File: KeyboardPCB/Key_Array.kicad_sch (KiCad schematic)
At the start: 70 parts

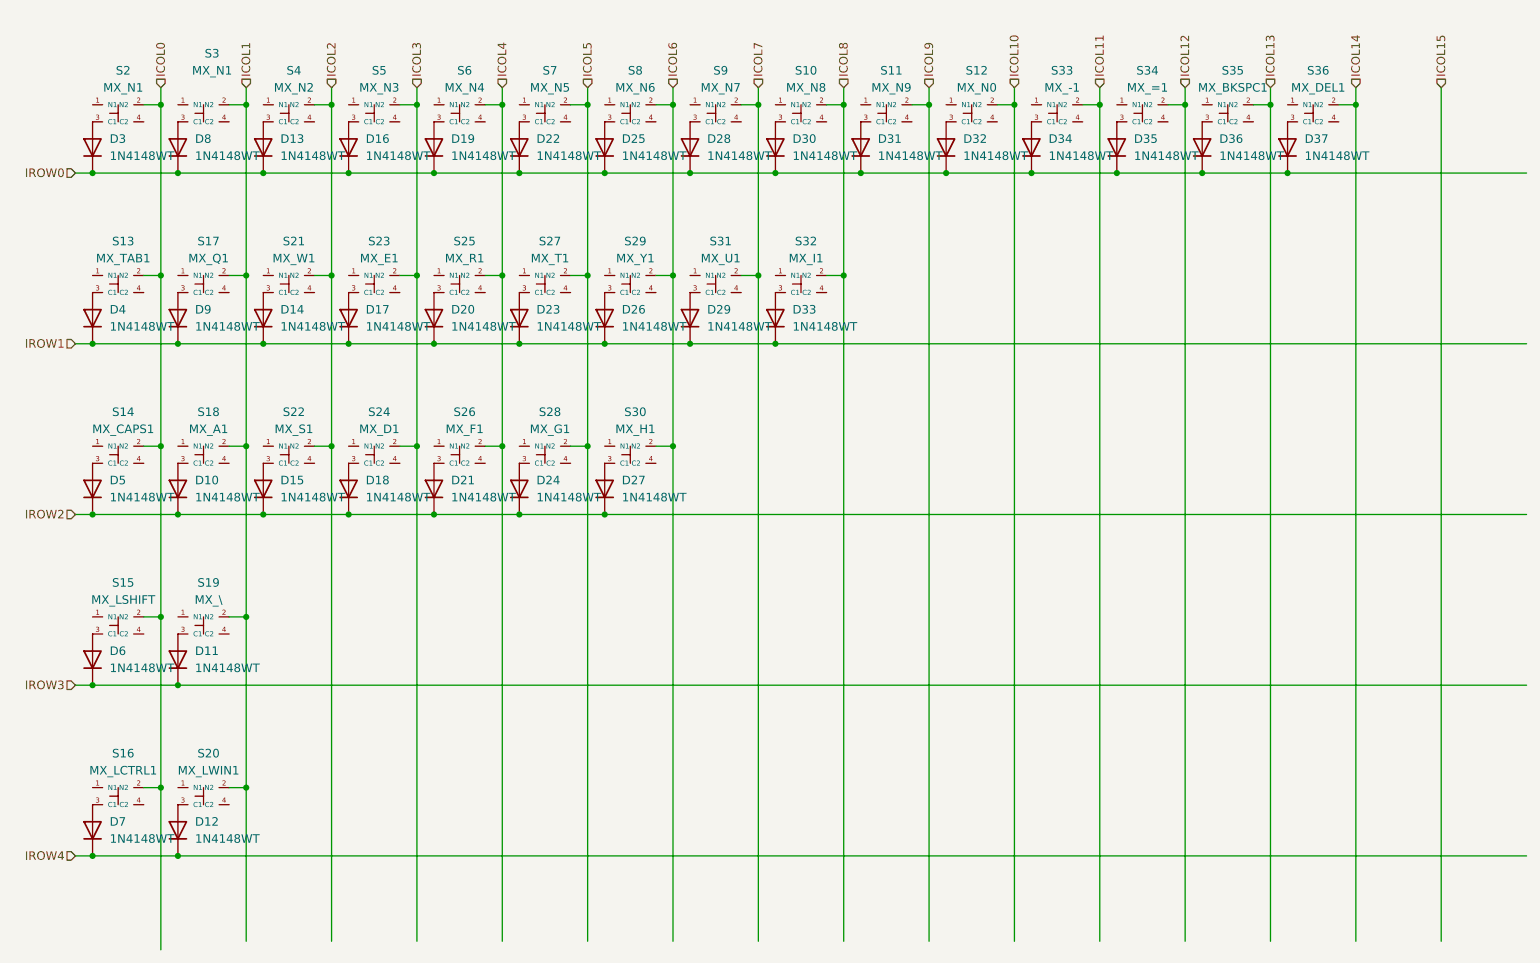
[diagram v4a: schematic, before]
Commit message: Made progress on the key matrix, and did some part substitutions
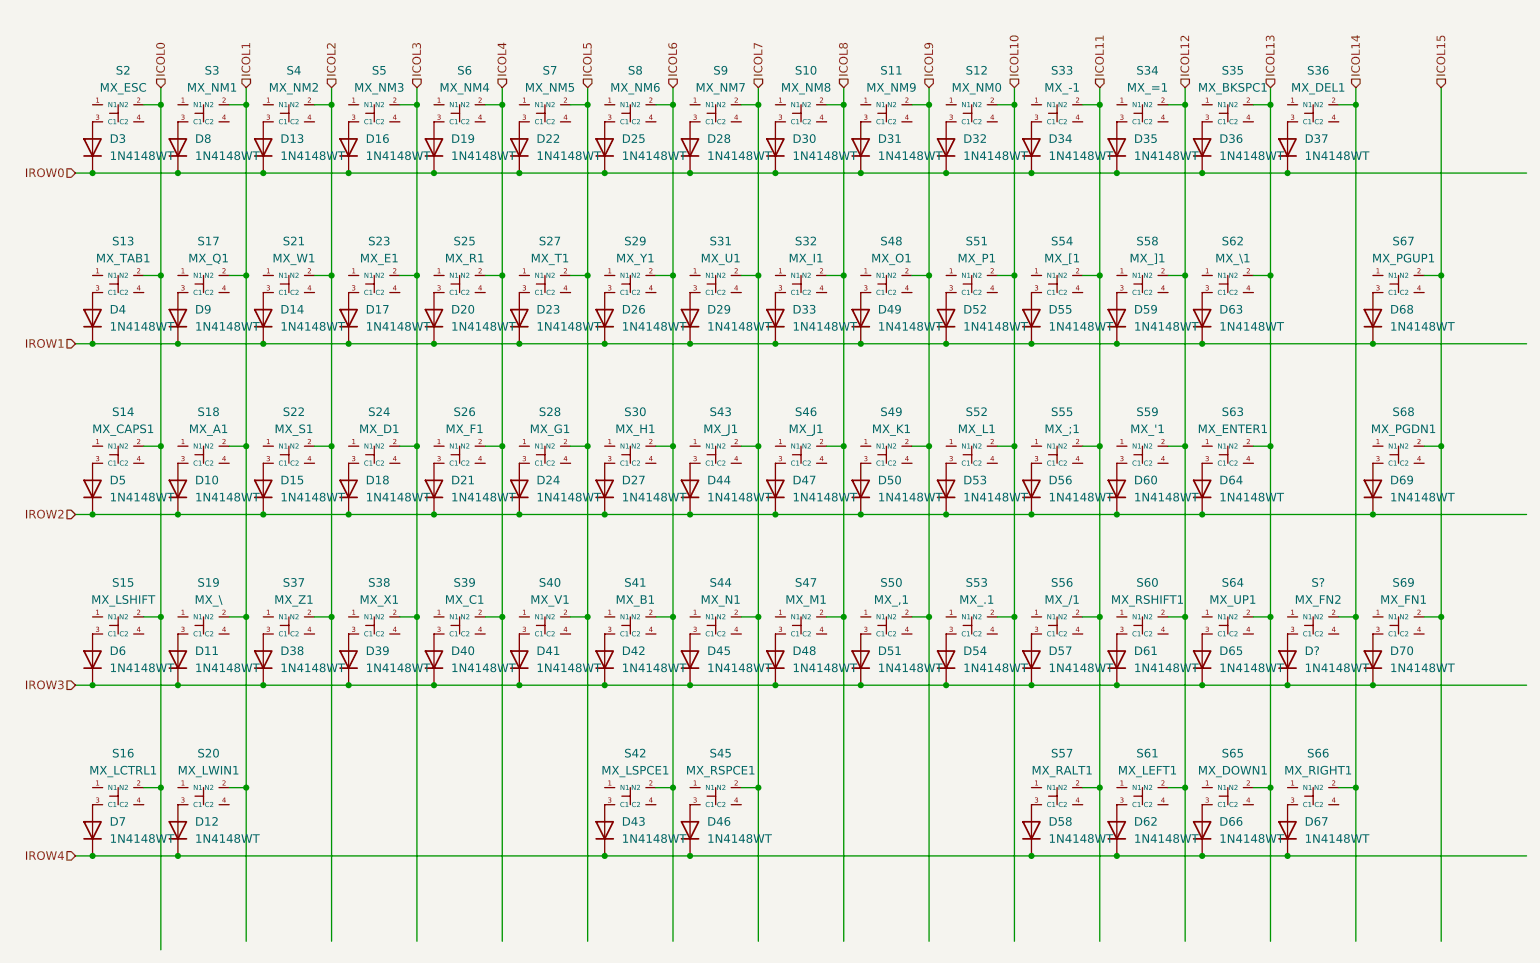
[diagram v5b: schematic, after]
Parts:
- added D38, D39, D40, D41, D42, D43, D44, D45, D46, D47, D48, D49, D50, D51, D52, D53, D54, D55, D56, D57, D58, D59, D60, D61, D62, D63, D64, D65, D66, D67, D68, D69, D70, D?: 1N4148WT, Diode_SMD:D_SOD-523, symbol Diode:1N4148WT
- added S37: MX_Z1, TS18525SL160SMTTR, symbol keyboard_syms:TS18-5-25-SL-160-SMT-TR
- added S38: MX_X1, TS18525SL160SMTTR, symbol keyboard_syms:TS18-5-25-SL-160-SMT-TR
- added S39: MX_C1, TS18525SL160SMTTR, symbol keyboard_syms:TS18-5-25-SL-160-SMT-TR
- added S40: MX_V1, TS18525SL160SMTTR, symbol keyboard_syms:TS18-5-25-SL-160-SMT-TR
- added S41: MX_B1, TS18525SL160SMTTR, symbol keyboard_syms:TS18-5-25-SL-160-SMT-TR
- added S42: MX_LSPCE1, TS18525SL160SMTTR, symbol keyboard_syms:TS18-5-25-SL-160-SMT-TR
- added S43, S46: MX_J1, TS18525SL160SMTTR, symbol keyboard_syms:TS18-5-25-SL-160-SMT-TR
- added S44: MX_N1, TS18525SL160SMTTR, symbol keyboard_syms:TS18-5-25-SL-160-SMT-TR
- added S45: MX_RSPCE1, TS18525SL160SMTTR, symbol keyboard_syms:TS18-5-25-SL-160-SMT-TR
- added S47: MX_M1, TS18525SL160SMTTR, symbol keyboard_syms:TS18-5-25-SL-160-SMT-TR
- added S48: MX_O1, TS18525SL160SMTTR, symbol keyboard_syms:TS18-5-25-SL-160-SMT-TR
- added S49: MX_K1, TS18525SL160SMTTR, symbol keyboard_syms:TS18-5-25-SL-160-SMT-TR
- added S50: MX_,1, TS18525SL160SMTTR, symbol keyboard_syms:TS18-5-25-SL-160-SMT-TR
- added S51: MX_P1, TS18525SL160SMTTR, symbol keyboard_syms:TS18-5-25-SL-160-SMT-TR
- added S52: MX_L1, TS18525SL160SMTTR, symbol keyboard_syms:TS18-5-25-SL-160-SMT-TR
- added S53: MX_.1, TS18525SL160SMTTR, symbol keyboard_syms:TS18-5-25-SL-160-SMT-TR
- added S54: MX_[1, TS18525SL160SMTTR, symbol keyboard_syms:TS18-5-25-SL-160-SMT-TR
- added S55: MX_;1, TS18525SL160SMTTR, symbol keyboard_syms:TS18-5-25-SL-160-SMT-TR
- added S56: MX_/1, TS18525SL160SMTTR, symbol keyboard_syms:TS18-5-25-SL-160-SMT-TR
- added S57: MX_RALT1, TS18525SL160SMTTR, symbol keyboard_syms:TS18-5-25-SL-160-SMT-TR
- added S58: MX_]1, TS18525SL160SMTTR, symbol keyboard_syms:TS18-5-25-SL-160-SMT-TR
- added S59: MX_'1, TS18525SL160SMTTR, symbol keyboard_syms:TS18-5-25-SL-160-SMT-TR
- added S60: MX_RSHIFT1, TS18525SL160SMTTR, symbol keyboard_syms:TS18-5-25-SL-160-SMT-TR
- added S61: MX_LEFT1, TS18525SL160SMTTR, symbol keyboard_syms:TS18-5-25-SL-160-SMT-TR
- added S62: MX_\1, TS18525SL160SMTTR, symbol keyboard_syms:TS18-5-25-SL-160-SMT-TR
- added S63: MX_ENTER1, TS18525SL160SMTTR, symbol keyboard_syms:TS18-5-25-SL-160-SMT-TR
- added S64: MX_UP1, TS18525SL160SMTTR, symbol keyboard_syms:TS18-5-25-SL-160-SMT-TR
- added S65: MX_DOWN1, TS18525SL160SMTTR, symbol keyboard_syms:TS18-5-25-SL-160-SMT-TR
- added S66: MX_RIGHT1, TS18525SL160SMTTR, symbol keyboard_syms:TS18-5-25-SL-160-SMT-TR
- added S67: MX_PGUP1, TS18525SL160SMTTR, symbol keyboard_syms:TS18-5-25-SL-160-SMT-TR
- added S68: MX_PGDN1, TS18525SL160SMTTR, symbol keyboard_syms:TS18-5-25-SL-160-SMT-TR
- added S69: MX_FN1, TS18525SL160SMTTR, symbol keyboard_syms:TS18-5-25-SL-160-SMT-TR
- added S?: MX_FN2, TS18525SL160SMTTR, symbol keyboard_syms:TS18-5-25-SL-160-SMT-TR
- S10: value MX_N8 -> MX_NM8
- S11: value MX_N9 -> MX_NM9
- S12: value MX_N0 -> MX_NM0
- S2: value MX_N1 -> MX_ESC
- S3: value MX_N1 -> MX_NM1
- S4: value MX_N2 -> MX_NM2
- S5: value MX_N3 -> MX_NM3
- S6: value MX_N4 -> MX_NM4
- S7: value MX_N5 -> MX_NM5
- S8: value MX_N6 -> MX_NM6
- S9: value MX_N7 -> MX_NM7
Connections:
- net ICOL10: now also S51.2 (N2), S52.2 (N2), S53.2 (N2)
- net ICOL11: now also S54.2 (N2), S55.2 (N2), S56.2 (N2), S57.2 (N2)
- net ICOL12: now also S58.2 (N2), S59.2 (N2), S60.2 (N2), S61.2 (N2)
- net ICOL13: now also S62.2 (N2), S63.2 (N2), S64.2 (N2), S65.2 (N2)
- net ICOL14: now also S66.2 (N2), S?.2 (N2)
- net ICOL15: now also S67.2 (N2), S68.2 (N2), S69.2 (N2)
- net ICOL2: now also S37.2 (N2)
- net ICOL3: now also S38.2 (N2)
- net ICOL4: now also S39.2 (N2)
- net ICOL5: now also S40.2 (N2)
- net ICOL6: now also S41.2 (N2), S42.2 (N2)
- net ICOL7: now also S43.2 (N2), S44.2 (N2), S45.2 (N2)
- net ICOL8: now also S46.2 (N2), S47.2 (N2)
- net ICOL9: now also S48.2 (N2), S49.2 (N2), S50.2 (N2)
- net IROW1: now also D49.1 (K), D52.1 (K), D55.1 (K), D59.1 (K), D63.1 (K), D68.1 (K)
- net IROW2: now also D44.1 (K), D47.1 (K), D50.1 (K), D53.1 (K), D56.1 (K), D60.1 (K), D64.1 (K), D69.1 (K)
- net IROW3: now also D38.1 (K), D39.1 (K), D40.1 (K), D41.1 (K), D42.1 (K), D45.1 (K), D48.1 (K), D51.1 (K), D54.1 (K), D57.1 (K), D61.1 (K), D65.1 (K), D70.1 (K), D?.1 (K)
- net IROW4: now also D43.1 (K), D46.1 (K), D58.1 (K), D62.1 (K), D66.1 (K), D67.1 (K)
- new net: D61.2 (A), S60.3 (C1)
- new net: D70.2 (A), S69.3 (C1)
- new net: D53.2 (A), S52.3 (C1)
- new net: D57.2 (A), S56.3 (C1)
- new net: D62.2 (A), S61.3 (C1)
- new net: D46.2 (A), S45.3 (C1)
- new net: D39.2 (A), S38.3 (C1)
- new net: D64.2 (A), S63.3 (C1)
- new net: D63.2 (A), S62.3 (C1)
- new net: D58.2 (A), S57.3 (C1)
- new net: D54.2 (A), S53.3 (C1)
- new net: D65.2 (A), S64.3 (C1)
- new net: D43.2 (A), S42.3 (C1)
- new net: D60.2 (A), S59.3 (C1)
- new net: D67.2 (A), S66.3 (C1)
- new net: D?.2 (A), S?.3 (C1)
- new net: D55.2 (A), S54.3 (C1)
- new net: D59.2 (A), S58.3 (C1)
- new net: D40.2 (A), S39.3 (C1)
- new net: D41.2 (A), S40.3 (C1)
- new net: D69.2 (A), S68.3 (C1)
- new net: D48.2 (A), S47.3 (C1)
- new net: D56.2 (A), S55.3 (C1)
- new net: D44.2 (A), S43.3 (C1)
- new net: D68.2 (A), S67.3 (C1)
- new net: D49.2 (A), S48.3 (C1)
- new net: D42.2 (A), S41.3 (C1)
- new net: D51.2 (A), S50.3 (C1)
- new net: D52.2 (A), S51.3 (C1)
- new net: D45.2 (A), S44.3 (C1)
- new net: D47.2 (A), S46.3 (C1)
- new net: D66.2 (A), S65.3 (C1)
- new net: D38.2 (A), S37.3 (C1)
- new net: D50.2 (A), S49.3 (C1)

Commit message: Added NCs
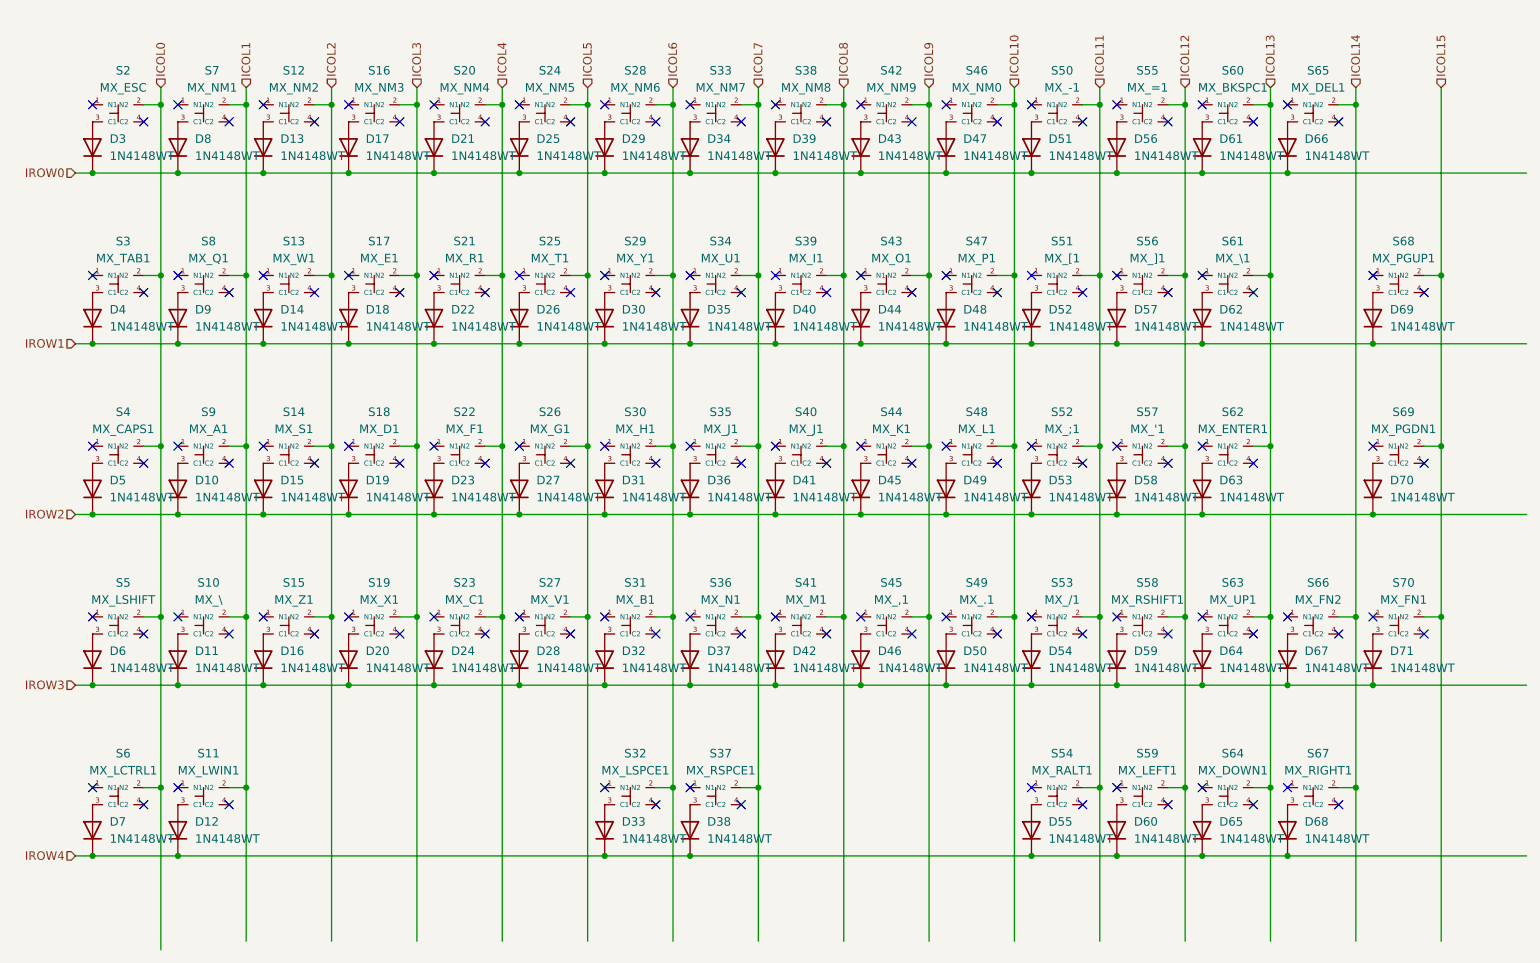
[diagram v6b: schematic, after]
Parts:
- gave numbers to parts that had none: 2
- renumbered D38 to D16, D16 to D17, D17 to D18, D18 to D19, D39 to D20, D19 to D21, D20 to D22, D21 to D23, D40 to D24, D22 to D25, D23 to D26, D24 to D27, D41 to D28, D25 to D29, D26 to D30, D27 to D31, D42 to D32, D43 to D33, D28 to D34, D29 to D35, D44 to D36, D45 to D37, D46 to D38, D30 to D39, D33 to D40, D47 to D41, D48 to D42, D31 to D43, D49 to D44, D50 to D45, D51 to D46, D32 to D47, D52 to D48, D53 to D49, D54 to D50, D34 to D51, D55 to D52, D56 to D53, D57 to D54, D58 to D55, D35 to D56, D59 to D57, D60 to D58, D61 to D59, D62 to D60, D36 to D61, D63 to D62, D64 to D63, D65 to D64, D66 to D65, D37 to D66, D67 to D68, D68 to D69, D69 to D70, D70 to D71, S19 to S10, S20 to S11, S4 to S12, S21 to S13, S22 to S14, S37 to S15, S5 to S16, S23 to S17, S24 to S18, S38 to S19, S6 to S20, S25 to S21, S26 to S22, S39 to S23, S7 to S24, S27 to S25, S28 to S26, S40 to S27, S8 to S28, S13 to S3, S41 to S31, S42 to S32, S9 to S33, S31 to S34, S43 to S35, S44 to S36, S45 to S37, S10 to S38, S32 to S39, S14 to S4, S46 to S40, S47 to S41, S11 to S42, S48 to S43, S49 to S44, S50 to S45, S12 to S46, S51 to S47, S52 to S48, S53 to S49, S15 to S5, S33 to S50, S54 to S51, S55 to S52, S56 to S53, S57 to S54, S34 to S55, S58 to S56, S59 to S57, S60 to S58, S61 to S59, S16 to S6, S35 to S60, S62 to S61, S63 to S62, S64 to S63, S65 to S64, S36 to S65, S66 to S67, S67 to S68, S68 to S69, S3 to S7, S69 to S70, S17 to S8, S18 to S9
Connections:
- no-connect marks 0 -> 138
